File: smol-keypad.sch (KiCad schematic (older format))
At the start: 39 parts, among them SW1 Rotary_Encoder_Switch, U1 ProMicro

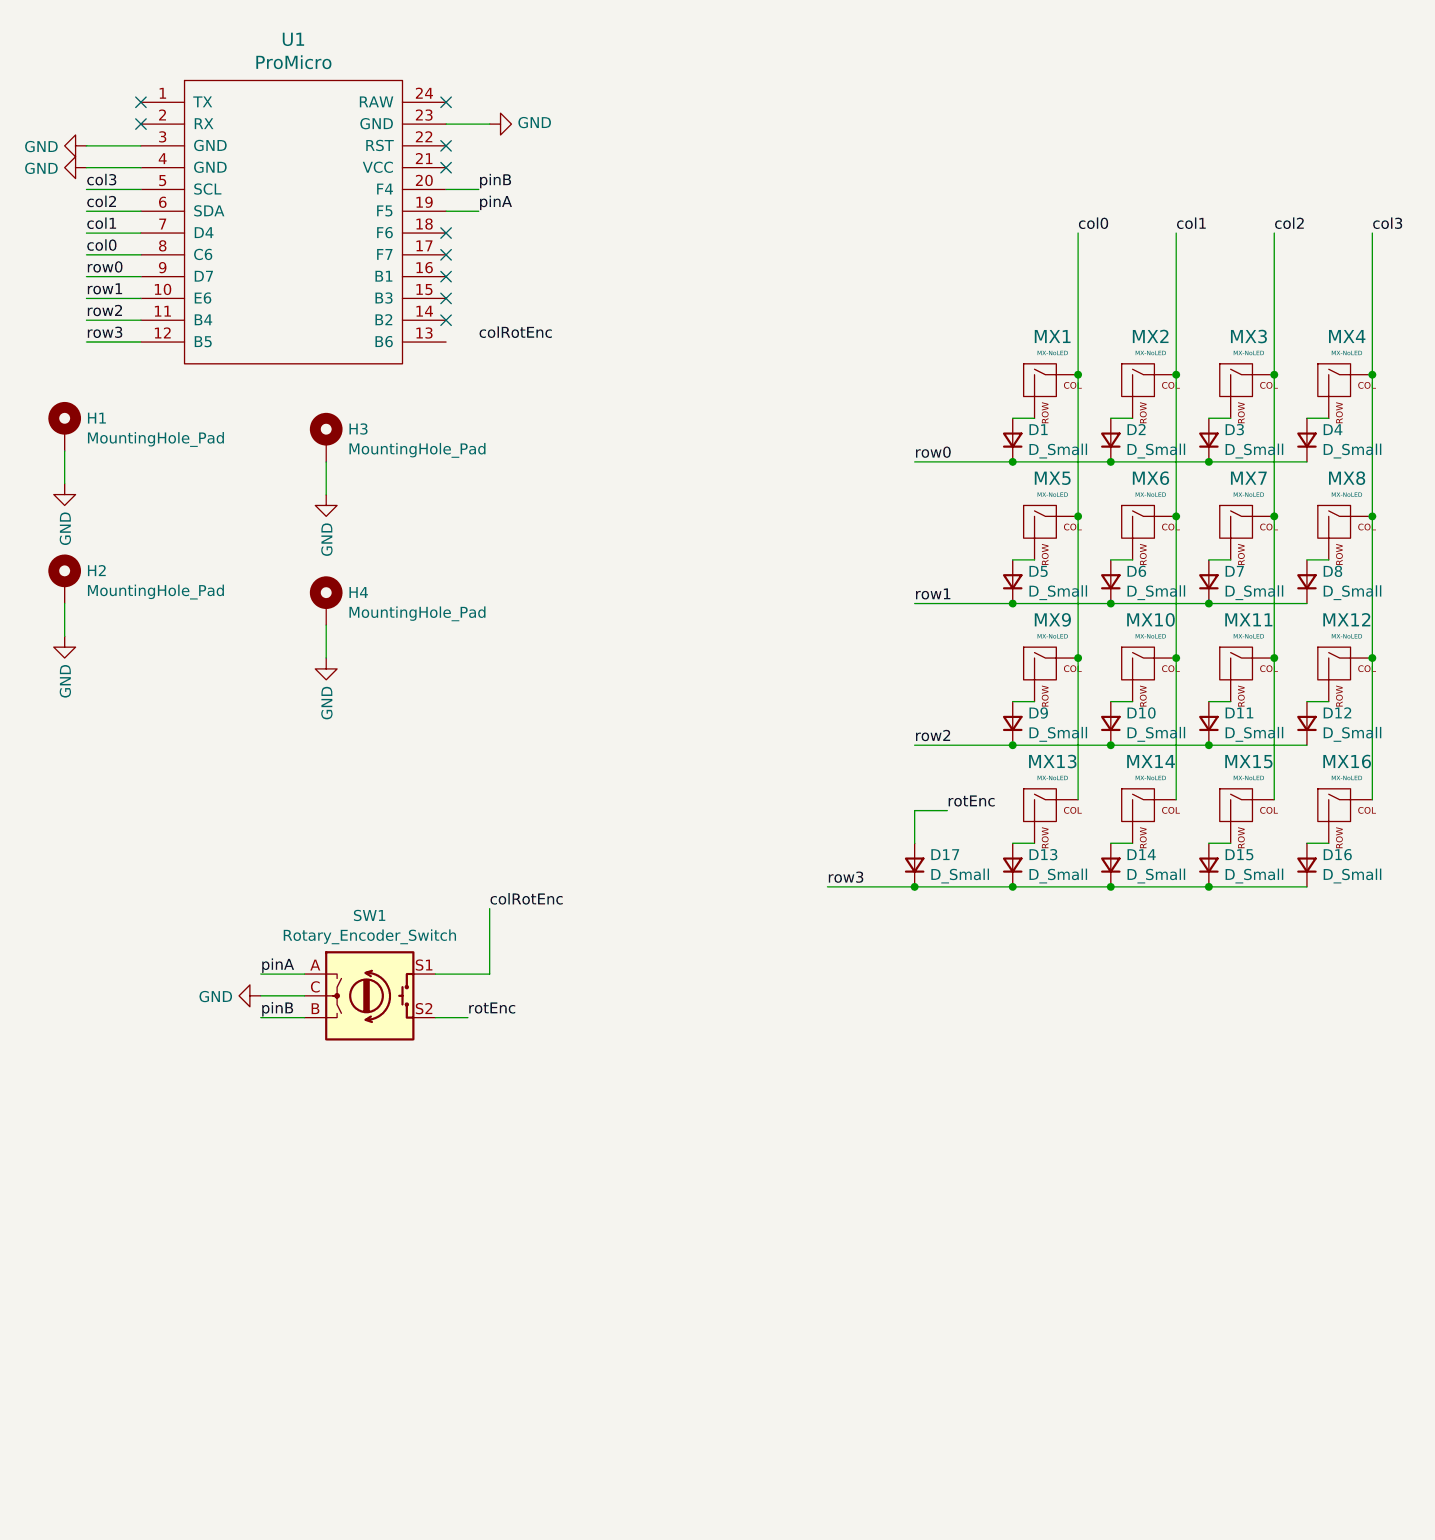
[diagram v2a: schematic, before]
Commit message: add kbd library
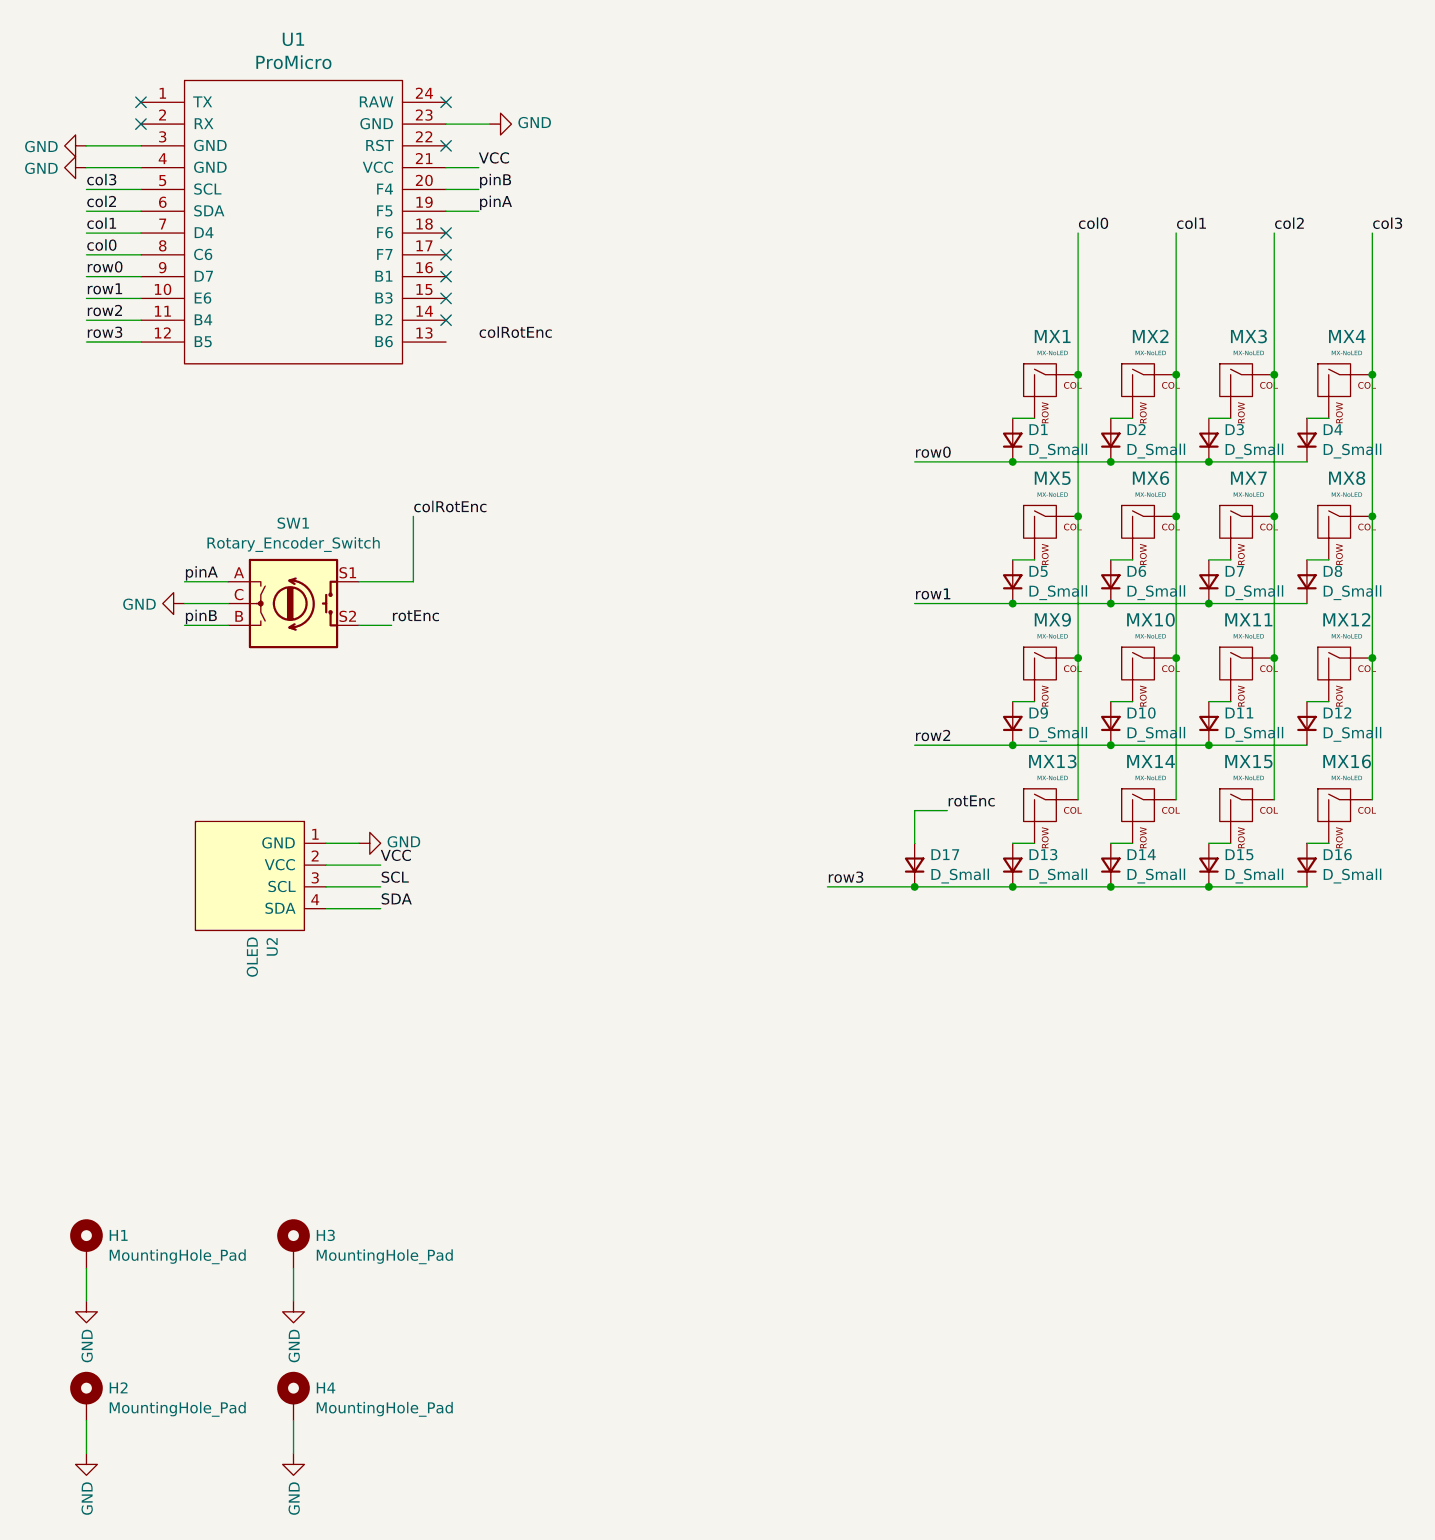
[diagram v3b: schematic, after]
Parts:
- added U2: OLED, Display:Adafruit_SSD1306, symbol SSD1306-128x64_OLED:OLED
- SW1: footprint Rotary_Encoder:RotaryEncoder_Alps_EC11E-Switch_Vertical_H20mm -> Keebio-Parts:RotaryEncoder_EC11
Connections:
- net GND: now also U2.1 (GND)
- net VCC: now reaches U1.21 (VCC)
- net VCC: now also U2.2 (VCC)
- new net SCL: U2.3 (SCL)
- new net SDA: U2.4 (SDA)
- no-connect marks 10 -> 9
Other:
- moved on the sheet: H1, H2, H3, H4, SW1
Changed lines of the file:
@@
 NoConn ~ 2550 1150
 NoConn ~ 2550 1350
-NoConn ~ 2550 1450
 NoConn ~ 2550 1750
 NoConn ~ 2550 1850
@@
 L Mechanical:MountingHole_Pad H2
 U 1 1 60AAE5B6
-P 800 3350
-F 0 "H2" H 900 3399 50  0000 L CNN
-F 1 "MountingHole_Pad" H 900 3308 50  0000 L CNN
-F 2 "MountingHole:MountingHole_2.2mm_M2_Pad" H 800 3350 50  0001 C CNN
-F 3 "~" H 800 3350 50  0001 C CNN
-	1    800  3350
+P 900 7100
+F 0 "H2" H 1000 7149 50  0000 L CNN
+F 1 "MountingHole_Pad" H 1000 7058 50  0000 L CNN
+F 2 "MountingHole:MountingHole_2.2mm_M2_Pad" H 900 7100 50  0001 C CNN
+F 3 "~" H 900 7100 50  0001 C CNN
+	1    900  7100
 	1    0    0    -1
 $EndComp
@@
 L power:GND #PWR0104
 U 1 1 60AB94B2
-P 800 3600
-F 0 "#PWR0104" H 800 3350 50  0001 C CNN
-F 1 "GND" V 805 3472 50  0000 R CNN
-F 2 "" H 800 3600 50  0001 C CNN
-F 3 "" H 800 3600 50  0001 C CNN
-	1    800  3600
-	1    0    0    -1
-$EndComp
-Wire Wire Line
-	800  3450 800  3600
+P 900 7350
+F 0 "#PWR0104" H 900 7100 50  0001 C CNN
+F 1 "GND" V 905 7222 50  0000 R CNN
+F 2 "" H 900 7350 50  0001 C CNN
+F 3 "" H 900 7350 50  0001 C CNN
+	1    900  7350
+	1    0    0    -1
+$EndComp
+Wire Wire Line
+	900  7200 900  7350
 $Comp
 L Mechanical:MountingHole_Pad H1
 U 1 1 60AC6A81
-P 800 2650
-F 0 "H1" H 900 2699 50  0000 L CNN
-F 1 "MountingHole_Pad" H 900 2608 50  0000 L CNN
-F 2 "MountingHole:MountingHole_2.2mm_M2_Pad" H 800 2650 50  0001 C CNN
-F 3 "~" H 800 2650 50  0001 C CNN
-	1    800  2650
+P 900 6400
+F 0 "H1" H 1000 6449 50  0000 L CNN
+F 1 "MountingHole_Pad" H 1000 6358 50  0000 L CNN
+F 2 "MountingHole:MountingHole_2.2mm_M2_Pad" H 900 6400 50  0001 C CNN
+F 3 "~" H 900 6400 50  0001 C CNN
+	1    900  6400
 	1    0    0    -1
 $EndComp
@@
 L power:GND #PWR0105
 U 1 1 60AC6A87
-P 800 2900
-F 0 "#PWR0105" H 800 2650 50  0001 C CNN
-F 1 "GND" V 805 2772 50  0000 R CNN
-F 2 "" H 800 2900 50  0001 C CNN
-F 3 "" H 800 2900 50  0001 C CNN
-	1    800  2900
-	1    0    0    -1
-$EndComp
-Wire Wire Line
-	800  2750 800  2900
+P 900 6650
+F 0 "#PWR0105" H 900 6400 50  0001 C CNN
+F 1 "GND" V 905 6522 50  0000 R CNN
+F 2 "" H 900 6650 50  0001 C CNN
+F 3 "" H 900 6650 50  0001 C CNN
+	1    900  6650
+	1    0    0    -1
+$EndComp
+Wire Wire Line
+	900  6500 900  6650
 $Comp
 L Mechanical:MountingHole_Pad H3
 U 1 1 60AC8526
-P 2000 2700
-F 0 "H3" H 2100 2749 50  0000 L CNN
-F 1 "MountingHole_Pad" H 2100 2658 50  0000 L CNN
-F 2 "MountingHole:MountingHole_2.2mm_M2_Pad" H 2000 2700 50  0001 C CNN
-F 3 "~" H 2000 2700 50  0001 C CNN
-	1    2000 2700
+P 1850 6400
+F 0 "H3" H 1950 6449 50  0000 L CNN
+F 1 "MountingHole_Pad" H 1950 6358 50  0000 L CNN
+F 2 "MountingHole:MountingHole_2.2mm_M2_Pad" H 1850 6400 50  0001 C CNN
+F 3 "~" H 1850 6400 50  0001 C CNN
+	1    1850 6400
 	1    0    0    -1
 $EndComp
@@
 L power:GND #PWR0106
 U 1 1 60AC852C
-P 2000 2950
-F 0 "#PWR0106" H 2000 2700 50  0001 C CNN
-F 1 "GND" V 2005 2822 50  0000 R CNN
-F 2 "" H 2000 2950 50  0001 C CNN
-F 3 "" H 2000 2950 50  0001 C CNN
-	1    2000 2950
-	1    0    0    -1
-$EndComp
-Wire Wire Line
-	2000 2800 2000 2950
+P 1850 6650
+F 0 "#PWR0106" H 1850 6400 50  0001 C CNN
+F 1 "GND" V 1855 6522 50  0000 R CNN
+F 2 "" H 1850 6650 50  0001 C CNN
+F 3 "" H 1850 6650 50  0001 C CNN
+	1    1850 6650
+	1    0    0    -1
+$EndComp
+Wire Wire Line
+	1850 6500 1850 6650
 $Comp
 L Mechanical:MountingHole_Pad H4
 U 1 1 60ACAC15
-P 2000 3450
-F 0 "H4" H 2100 3499 50  0000 L CNN
-F 1 "MountingHole_Pad" H 2100 3408 50  0000 L CNN
-F 2 "MountingHole:MountingHole_2.2mm_M2_Pad" H 2000 3450 50  0001 C CNN
-F 3 "~" H 2000 3450 50  0001 C CNN
-	1    2000 3450
+P 1850 7100
+F 0 "H4" H 1950 7149 50  0000 L CNN
+F 1 "MountingHole_Pad" H 1950 7058 50  0000 L CNN
+F 2 "MountingHole:MountingHole_2.2mm_M2_Pad" H 1850 7100 50  0001 C CNN
+F 3 "~" H 1850 7100 50  0001 C CNN
+	1    1850 7100
 	1    0    0    -1
 $EndComp
@@
 L power:GND #PWR0107
 U 1 1 60ACAC1B
-P 2000 3700
-F 0 "#PWR0107" H 2000 3450 50  0001 C CNN
-F 1 "GND" V 2005 3572 50  0000 R CNN
-F 2 "" H 2000 3700 50  0001 C CNN
-F 3 "" H 2000 3700 50  0001 C CNN
-	1    2000 3700
-	1    0    0    -1
-$EndComp
-Wire Wire Line
-	2000 3550 2000 3700
+P 1850 7350
+F 0 "#PWR0107" H 1850 7100 50  0001 C CNN
+F 1 "GND" V 1855 7222 50  0000 R CNN
+F 2 "" H 1850 7350 50  0001 C CNN
+F 3 "" H 1850 7350 50  0001 C CNN
+	1    1850 7350
+	1    0    0    -1
+$EndComp
+Wire Wire Line
+	1850 7200 1850 7350
 Text Label 2700 1650 0    50   ~ 0
 pinA
@@
 $EndComp
 Wire Wire Line
-	1900 5150 1700 5150
-Wire Wire Line
-	1900 5350 1700 5350
-Text Label 1700 5350 0    50   ~ 0
+	1550 3350 1350 3350
+Wire Wire Line
+	1550 3550 1350 3550
+Text Label 1350 3550 0    50   ~ 0
 pinB
-Text Label 1700 5150 0    50   ~ 0
+Text Label 1350 3350 0    50   ~ 0
 pinA
 Wire Wire Line
-	1900 5250 1700 5250
+	1550 3450 1350 3450
 $Comp
 L power:GND #PWR0108
 U 1 1 60B4E820
-P 1700 5250
-F 0 "#PWR0108" H 1700 5000 50  0001 C CNN
-F 1 "GND" V 1705 5122 50  0000 R CNN
-F 2 "" H 1700 5250 50  0001 C CNN
-F 3 "" H 1700 5250 50  0001 C CNN
-	1    1700 5250
+P 1350 3450
+F 0 "#PWR0108" H 1350 3200 50  0001 C CNN
+F 1 "GND" V 1355 3322 50  0000 R CNN
+F 2 "" H 1350 3450 50  0001 C CNN
+F 3 "" H 1350 3450 50  0001 C CNN
+	1    1350 3450
 	0    1    1    0
 $EndComp
@@
 L Device:Rotary_Encoder_Switch SW1
 U 1 1 60B0022B
-P 2200 5250
-F 0 "SW1" H 2200 5617 50  0000 C CNN
-F 1 "Rotary_Encoder_Switch" H 2200 5526 50  0000 C CNN
-F 2 "Rotary_Encoder:RotaryEncoder_Alps_EC11E-Switch_Vertical_H20mm" H 2050 5410 50  0001 C CNN
-F 3 "~" H 2200 5510 50  0001 C CNN
-	1    2200 5250
+P 1850 3450
+F 0 "SW1" H 1850 3817 50  0000 C CNN
+F 1 "Rotary_Encoder_Switch" H 1850 3726 50  0000 C CNN
+F 2 "Keebio-Parts:RotaryEncoder_EC11" H 1700 3610 50  0001 C CNN
+F 3 "~" H 1850 3710 50  0001 C CNN
+	1    1850 3450
 	1    0    0    -1
 $EndComp
@@
 	4700 4400 4850 4400
 Wire Wire Line
-	2500 5350 2650 5350
-Text Label 2650 5350 0    50   ~ 0
+	2150 3550 2300 3550
+Text Label 2300 3550 0    50   ~ 0
 rotEnc
 Wire Wire Line
-	2500 5150 2750 5150
-Wire Wire Line
-	2750 5150 2750 4850
-Text Label 2750 4850 0    50   ~ 0
+	2150 3350 2400 3350
+Wire Wire Line
+	2400 3350 2400 3050
+Text Label 2400 3050 0    50   ~ 0
 colRotEnc
 Text Label 2700 2250 0    50   ~ 0
 colRotEnc
+$Comp
+L SSD1306-128x64_OLED:OLED U2
+U 1 1 60C2E002
+P 1650 4700
+F 0 "U2" H 1928 4804 50  0000 L CNN
+F 1 "OLED" H 1928 4713 50  0000 L CNN
+F 2 "Display:Adafruit_SSD1306" H 1650 4950 50  0001 C CNN
+F 3 "" H 1650 4950 50  0001 C CNN
+	1    1650 4700
+	0    1    1    0
+$EndComp
+$Comp
+L power:GND #PWR0109
+U 1 1 60C318F9
+P 2150 4550
+F 0 "#PWR0109" H 2150 4300 50  0001 C CNN
+F 1 "GND" V 2155 4422 50  0000 R CNN
+F 2 "" H 2150 4550 50  0001 C CNN
+F 3 "" H 2150 4550 50  0001 C CNN
+	1    2150 4550
+	0    -1   -1   0
+$EndComp
+Wire Wire Line
+	2000 4550 2150 4550
+Wire Wire Line
+	2550 1450 2700 1450
+Text Label 2700 1450 0    50   ~ 0
+VCC
+Text Label 2250 4650 0    50   ~ 0
+VCC
+Wire Wire Line
+	2000 4650 2250 4650
+Text Label 2250 4750 0    50   ~ 0
+SCL
+Text Label 2250 4850 0    50   ~ 0
+SDA
+Wire Wire Line
+	2000 4750 2250 4750
+Wire Wire Line
+	2250 4850 2000 4850
 $EndSCHEMATC
